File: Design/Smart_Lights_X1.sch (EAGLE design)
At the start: 35 parts, among them IC1 MP1584EN-LF-Z, J1 POWER_JACK, Q1 IRLR2905TRPBF, U1 ESP-32S

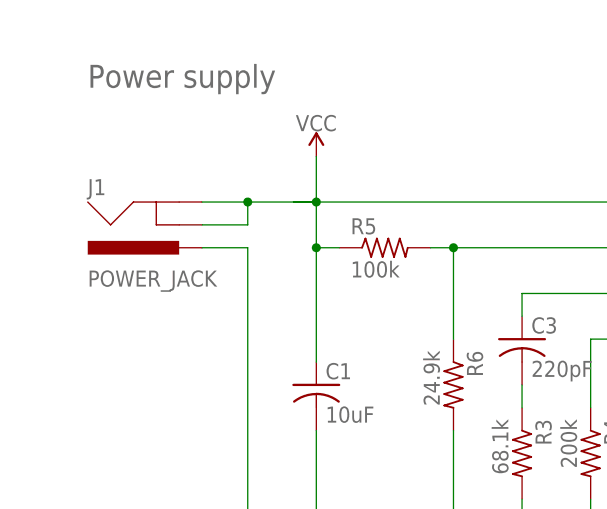
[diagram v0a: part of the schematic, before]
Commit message: Fixed DC Jack connection
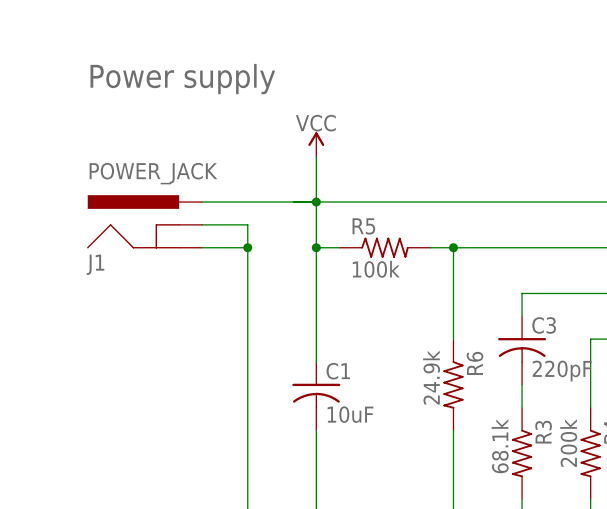
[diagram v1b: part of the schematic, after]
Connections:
- net GND: now also J1.GND, J1.GNDBREAK; no longer J1.PWR
- net VCC: now also J1.PWR; no longer J1.GND, J1.GNDBREAK
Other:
- moved on the sheet: J1
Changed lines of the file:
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@@
 <attribute name="VALUE" x="113.792" y="124.46" size="1.778" layer="96" font="vector" rot="R90" align="top-left"/>
 </instance>
-<instance part="J1" gate="G$1" x="22.86" y="157.48" smashed="yes" rot="MR180">
-<attribute name="VALUE" x="12.7" y="147.32" size="1.778" layer="96" font="vector" rot="MR180"/>
-<attribute name="NAME" x="12.7" y="157.48" size="1.778" layer="95" font="vector" rot="MR180"/>
+<instance part="J1" gate="G$1" x="22.86" y="147.32" smashed="yes">
+<attribute name="VALUE" x="12.7" y="157.48" size="1.778" layer="96" font="vector"/>
+<attribute name="NAME" x="12.7" y="147.32" size="1.778" layer="95" font="vector"/>
 </instance>
 <instance part="GND10" gate="1" x="30.48" y="116.84" smashed="yes">
@@
 </segment>
 <segment>
-<pinref part="J1" gate="G$1" pin="PWR"/>
+<wire x1="30.48" y1="152.4" x2="30.48" y2="149.86" width="0.1524" layer="91"/>
+<pinref part="GND10" gate="1" pin="GND"/>
+<pinref part="J1" gate="G$1" pin="GNDBREAK"/>
+<wire x1="30.48" y1="149.86" x2="30.48" y2="119.38" width="0.1524" layer="91"/>
+<wire x1="25.4" y1="152.4" x2="30.48" y2="152.4" width="0.1524" layer="91"/>
+<pinref part="J1" gate="G$1" pin="GND"/>
 <wire x1="25.4" y1="149.86" x2="30.48" y2="149.86" width="0.1524" layer="91"/>
-<wire x1="30.48" y1="149.86" x2="30.48" y2="119.38" width="0.1524" layer="91"/>
-<pinref part="GND10" gate="1" pin="GND"/>
+<junction x="30.48" y="149.86"/>
 </segment>
 </net>
@@
 <wire x1="38.1" y1="154.94" x2="35.56" y2="154.94" width="0.1524" layer="91"/>
 <junction x="38.1" y="154.94"/>
-<pinref part="J1" gate="G$1" pin="GNDBREAK"/>
-<wire x1="25.4" y1="152.4" x2="30.48" y2="152.4" width="0.1524" layer="91"/>
-<wire x1="30.48" y1="152.4" x2="30.48" y2="154.94" width="0.1524" layer="91"/>
-<wire x1="30.48" y1="154.94" x2="38.1" y2="154.94" width="0.1524" layer="91"/>
-<pinref part="J1" gate="G$1" pin="GND"/>
-<wire x1="25.4" y1="154.94" x2="30.48" y2="154.94" width="0.1524" layer="91"/>
-<junction x="30.48" y="154.94"/>
+<wire x1="25.4" y1="154.94" x2="38.1" y2="154.94" width="0.1524" layer="91"/>
 <pinref part="SUPPLY4" gate="G$1" pin="VCC"/>
 <wire x1="38.1" y1="160.02" x2="38.1" y2="154.94" width="0.1524" layer="91"/>
-</segment>
-</net>
+<pinref part="J1" gate="G$1" pin="PWR"/>
+</segment>
+</net>
